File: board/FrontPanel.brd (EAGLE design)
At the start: 76.2 x 44.5 mm, 10 parts, among them J1 PINHD-1X2BIG

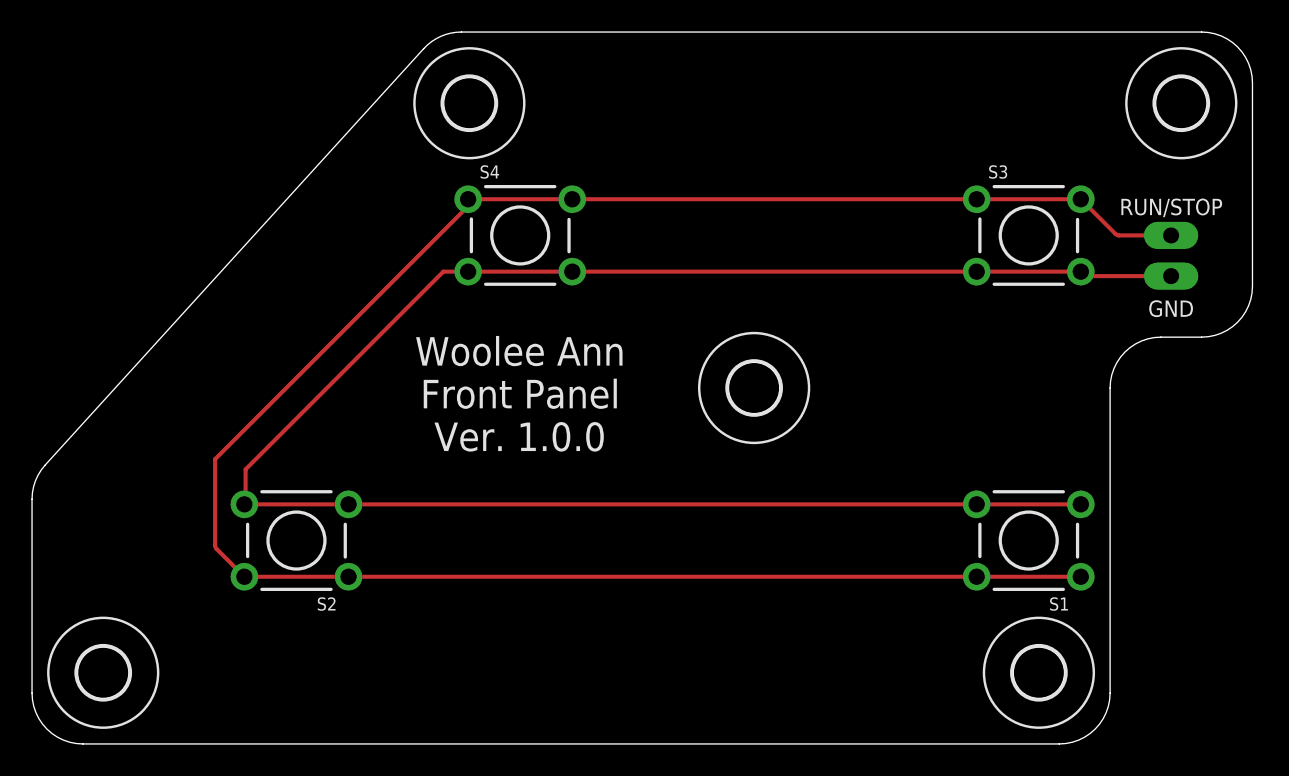
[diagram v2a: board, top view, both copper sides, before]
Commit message: Adjust front panel layout
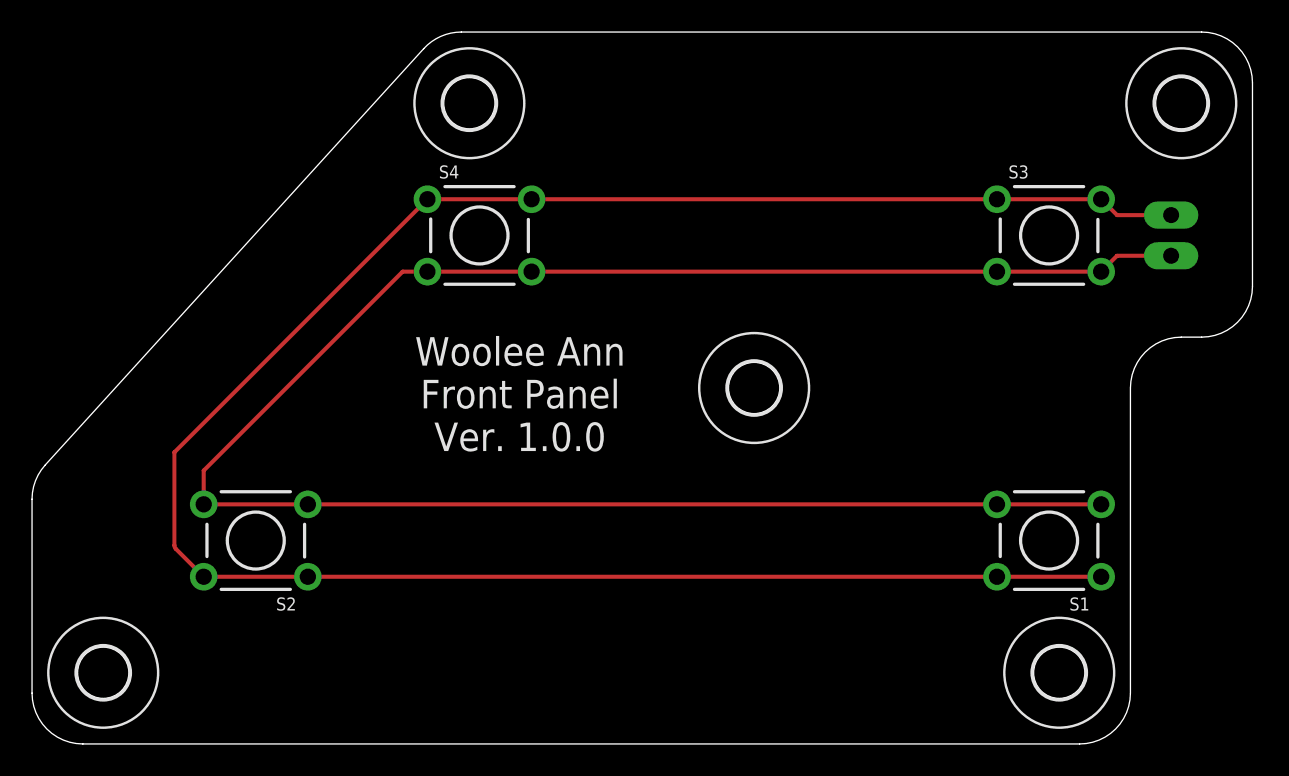
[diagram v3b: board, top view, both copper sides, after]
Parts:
- moved S2 2.54 mm to (14.0, 12.7)
- moved S4 2.54 mm to (27.9, 31.8)
- moved S1 1.27 mm to (63.5, 12.7)
- moved S3 1.27 mm to (63.5, 31.8)
- moved U$2 1.27 mm to (64.1, 4.45)
- moved J1 1.27 mm to (71.1, 31.8)
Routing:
- net N$2: track 117.4 -> 124.2 mm
- net N$1: track 127.9 -> 133.7 mm
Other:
- outline, holes or cut-outs redrawn
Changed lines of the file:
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@@
 <setting verticaltext="up"/>
 </settings>
-<grid distance="0.05" unitdist="inch" unit="inch" style="lines" multiple="1" display="yes" altdistance="0.025" altunitdist="inch" altunit="inch"/>
+<grid distance="0.05" unitdist="inch" unit="inch" style="lines" multiple="2" display="yes" altdistance="0.025" altunitdist="inch" altunit="inch"/>
 <layers>
 <layer number="1" name="Top" color="4" fill="1" visible="yes" active="yes"/>
@@
 <wire x1="0" y1="15.282521875" x2="0" y2="3.175" width="0" layer="20"/>
 <wire x1="0" y1="3.175" x2="3.175" y2="0" width="0" layer="20" curve="90"/>
-<wire x1="3.175" y1="0" x2="64.135" y2="0" width="0" layer="20"/>
-<wire x1="64.135" y1="0" x2="67.31" y2="3.175" width="0" layer="20" curve="90"/>
-<wire x1="67.31" y1="3.175" x2="67.31" y2="22.225" width="0" layer="20"/>
-<wire x1="67.31" y1="22.225" x2="70.485" y2="25.4" width="0" layer="20" curve="-90"/>
-<wire x1="70.485" y1="25.4" x2="73.025" y2="25.4" width="0" layer="20"/>
+<wire x1="3.175" y1="0" x2="65.405" y2="0" width="0" layer="20"/>
+<wire x1="65.405" y1="0" x2="68.58" y2="3.175" width="0" layer="20" curve="90"/>
+<wire x1="68.58" y1="3.175" x2="68.58" y2="22.225" width="0" layer="20"/>
+<wire x1="68.58" y1="22.225" x2="71.755" y2="25.4" width="0" layer="20" curve="-90"/>
+<wire x1="71.755" y1="25.4" x2="73.025" y2="25.4" width="0" layer="20"/>
 <wire x1="73.025" y1="25.4" x2="76.2" y2="28.575" width="0" layer="20" curve="90"/>
-<text x="71.12" y="33.02" size="1.016" layer="121" align="bottom-center">RUN/STOP</text>
-<text x="71.12" y="26.67" size="1.016" layer="121" align="bottom-center">GND</text>
+<text x="71.12" y="34.29" size="1.016" layer="122" rot="MR0" align="bottom-center">RUN/STOP</text>
+<text x="71.12" y="27.94" size="1.016" layer="122" rot="MR0" align="bottom-center">GND</text>
 <text x="30.48" y="25.4" size="1.778" layer="121" align="top-center">Woolee Ann
 Front Panel
@@
 </autorouter>
 <elements>
-<element name="S1" library="SaintGimp" package="TACTILE-SWITCH-6MM" value="SWITCH-MOMENTARY-6MM" x="62.23" y="12.7" rot="R180"/>
-<element name="S2" library="SaintGimp" package="TACTILE-SWITCH-6MM" value="SWITCH-MOMENTARY-6MM" x="16.51" y="12.7" rot="R180"/>
-<element name="S3" library="SaintGimp" package="TACTILE-SWITCH-6MM" value="SWITCH-MOMENTARY-6MM" x="62.23" y="31.75"/>
-<element name="S4" library="SaintGimp" package="TACTILE-SWITCH-6MM" value="SWITCH-MOMENTARY-6MM" x="30.48" y="31.75"/>
-<element name="J1" library="SaintGimp" package="1X02-BIG" value="PINHD-1X2BIG" x="71.12" y="30.48" smashed="yes" rot="R270"/>
+<element name="S1" library="SaintGimp" package="TACTILE-SWITCH-6MM" value="SWITCH-MOMENTARY-6MM" x="63.5" y="12.7" rot="R180"/>
+<element name="S2" library="SaintGimp" package="TACTILE-SWITCH-6MM" value="SWITCH-MOMENTARY-6MM" x="13.97" y="12.7" rot="R180"/>
+<element name="S3" library="SaintGimp" package="TACTILE-SWITCH-6MM" value="SWITCH-MOMENTARY-6MM" x="63.5" y="31.75"/>
+<element name="S4" library="SaintGimp" package="TACTILE-SWITCH-6MM" value="SWITCH-MOMENTARY-6MM" x="27.94" y="31.75"/>
+<element name="J1" library="SaintGimp" package="1X02-BIG" value="PINHD-1X2BIG" x="71.12" y="31.75" smashed="yes" rot="R270"/>
 <element name="U$1" library="holes" package="3,2" value="" x="4.445" y="4.445"/>
-<element name="U$2" library="holes" package="3,2" value="" x="62.865" y="4.445"/>
+<element name="U$2" library="holes" package="3,2" value="" x="64.135" y="4.445"/>
 <element name="U$3" library="holes" package="3,2" value="" x="27.305" y="40.005"/>
 <element name="U$4" library="holes" package="3,2" value="" x="71.755" y="40.005"/>
@@
 <contactref element="S4" pad="1"/>
 <contactref element="S4" pad="2"/>
-<wire x1="71.12" y1="31.75" x2="67.8733125" y2="31.75" width="0.254" layer="1"/>
-<wire x1="67.8733125" y1="31.75" x2="67.64880625" y2="31.84299375" width="0.254" layer="1" curve="-45"/>
-<wire x1="67.64880625" y1="31.84299375" x2="65.4812" y2="34.0106" width="0.254" layer="1"/>
-<wire x1="65.4812" y1="34.0106" x2="58.9788" y2="34.0106" width="0.254" layer="1"/>
-<wire x1="58.9788" y1="34.0106" x2="33.7312" y2="34.0106" width="0.254" layer="1"/>
-<wire x1="33.7312" y1="34.0106" x2="27.2288" y2="34.0106" width="0.254" layer="1"/>
-<wire x1="27.2288" y1="34.0106" x2="27.2288" y2="33.7103125" width="0.254" layer="1"/>
-<wire x1="27.2288" y1="33.7103125" x2="27.13580625" y2="33.48580625" width="0.254" layer="1" curve="-45"/>
-<wire x1="27.13580625" y1="33.48580625" x2="11.43" y2="17.78" width="0.254" layer="1"/>
-<wire x1="11.43" y1="17.78" x2="11.43" y2="12.3997125" width="0.254" layer="1"/>
-<wire x1="11.43" y1="12.3997125" x2="11.52299375" y2="12.17520625" width="0.254" layer="1" curve="45"/>
-<wire x1="11.52299375" y1="12.17520625" x2="13.2588" y2="10.4394" width="0.254" layer="1"/>
-<wire x1="13.2588" y1="10.4394" x2="19.7612" y2="10.4394" width="0.254" layer="1"/>
-<wire x1="58.9788" y1="10.4394" x2="19.7612" y2="10.4394" width="0.254" layer="1"/>
-<wire x1="58.9788" y1="10.4394" x2="65.4812" y2="10.4394" width="0.254" layer="1"/>
+<wire x1="66.7512" y1="34.0106" x2="60.2488" y2="34.0106" width="0.254" layer="1"/>
+<wire x1="60.2488" y1="34.0106" x2="31.1912" y2="34.0106" width="0.254" layer="1"/>
+<wire x1="31.1912" y1="34.0106" x2="24.6888" y2="34.0106" width="0.254" layer="1"/>
+<wire x1="8.89" y1="18.2118" x2="8.89" y2="12.3997125" width="0.254" layer="1"/>
+<wire x1="8.89" y1="12.3997125" x2="8.98299375" y2="12.17520625" width="0.254" layer="1" curve="45"/>
+<wire x1="8.98299375" y1="12.17520625" x2="10.7188" y2="10.4394" width="0.254" layer="1"/>
+<wire x1="10.7188" y1="10.4394" x2="17.2212" y2="10.4394" width="0.254" layer="1"/>
+<wire x1="60.2488" y1="10.4394" x2="17.2212" y2="10.4394" width="0.254" layer="1"/>
+<wire x1="60.2488" y1="10.4394" x2="66.7512" y2="10.4394" width="0.254" layer="1"/>
+<wire x1="71.12" y1="33.02" x2="67.7418" y2="33.02" width="0.254" layer="1"/>
+<wire x1="67.7418" y1="33.02" x2="66.7512" y2="34.0106" width="0.254" layer="1"/>
+<wire x1="24.6888" y1="34.0106" x2="8.89" y2="18.2118" width="0.254" layer="1"/>
 </signal>
 <signal name="N$2">
@@
 <contactref element="S1" pad="3"/>
 <contactref element="J1" pad="2"/>
-<wire x1="71.12" y1="29.21" x2="65.8921125" y2="29.21" width="0.254" layer="1"/>
-<wire x1="65.8921125" y1="29.21" x2="65.66760625" y2="29.30299375" width="0.254" layer="1" curve="-45"/>
-<wire x1="65.66760625" y1="29.30299375" x2="65.4812" y2="29.4894" width="0.254" layer="1"/>
-<wire x1="65.4812" y1="29.4894" x2="58.9788" y2="29.4894" width="0.254" layer="1"/>
-<wire x1="58.9788" y1="29.4894" x2="33.7312" y2="29.4894" width="0.254" layer="1"/>
-<wire x1="33.7312" y1="29.4894" x2="27.2288" y2="29.4894" width="0.254" layer="1"/>
-<wire x1="13.2588" y1="14.9606" x2="19.7612" y2="14.9606" width="0.254" layer="1"/>
-<wire x1="58.9788" y1="14.9606" x2="19.7612" y2="14.9606" width="0.254" layer="1"/>
-<wire x1="58.9788" y1="14.9606" x2="65.4812" y2="14.9606" width="0.254" layer="1"/>
-<wire x1="27.2288" y1="29.4894" x2="25.6794" y2="29.4894" width="0.254" layer="1"/>
-<wire x1="25.6794" y1="29.4894" x2="13.335" y2="17.145" width="0.254" layer="1"/>
-<wire x1="13.335" y1="17.145" x2="13.335" y2="15.0368" width="0.254" layer="1"/>
-<wire x1="13.335" y1="15.0368" x2="13.2588" y2="14.9606" width="0.254" layer="1"/>
+<wire x1="66.7512" y1="29.4894" x2="60.2488" y2="29.4894" width="0.254" layer="1"/>
+<wire x1="60.2488" y1="29.4894" x2="31.1912" y2="29.4894" width="0.254" layer="1"/>
+<wire x1="31.1912" y1="29.4894" x2="24.6888" y2="29.4894" width="0.254" layer="1"/>
+<wire x1="10.7188" y1="14.9606" x2="17.2212" y2="14.9606" width="0.254" layer="1"/>
+<wire x1="60.2488" y1="14.9606" x2="17.2212" y2="14.9606" width="0.254" layer="1"/>
+<wire x1="60.2488" y1="14.9606" x2="66.7512" y2="14.9606" width="0.254" layer="1"/>
+<wire x1="10.795" y1="15.0368" x2="10.7188" y2="14.9606" width="0.254" layer="1"/>
+<wire x1="71.12" y1="30.48" x2="67.7418" y2="30.48" width="0.254" layer="1"/>
+<wire x1="67.7418" y1="30.48" x2="66.7512" y2="29.4894" width="0.254" layer="1"/>
+<wire x1="24.6888" y1="29.4894" x2="23.1394" y2="29.4894" width="0.254" layer="1"/>
+<wire x1="23.1394" y1="29.4894" x2="10.7188" y2="17.0688" width="0.254" layer="1"/>
+<wire x1="10.7188" y1="17.0688" x2="10.7188" y2="14.9606" width="0.254" layer="1"/>
 </signal>
 </signals>

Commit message: Spread out front panel buttons, flip terminal silkscreen to back
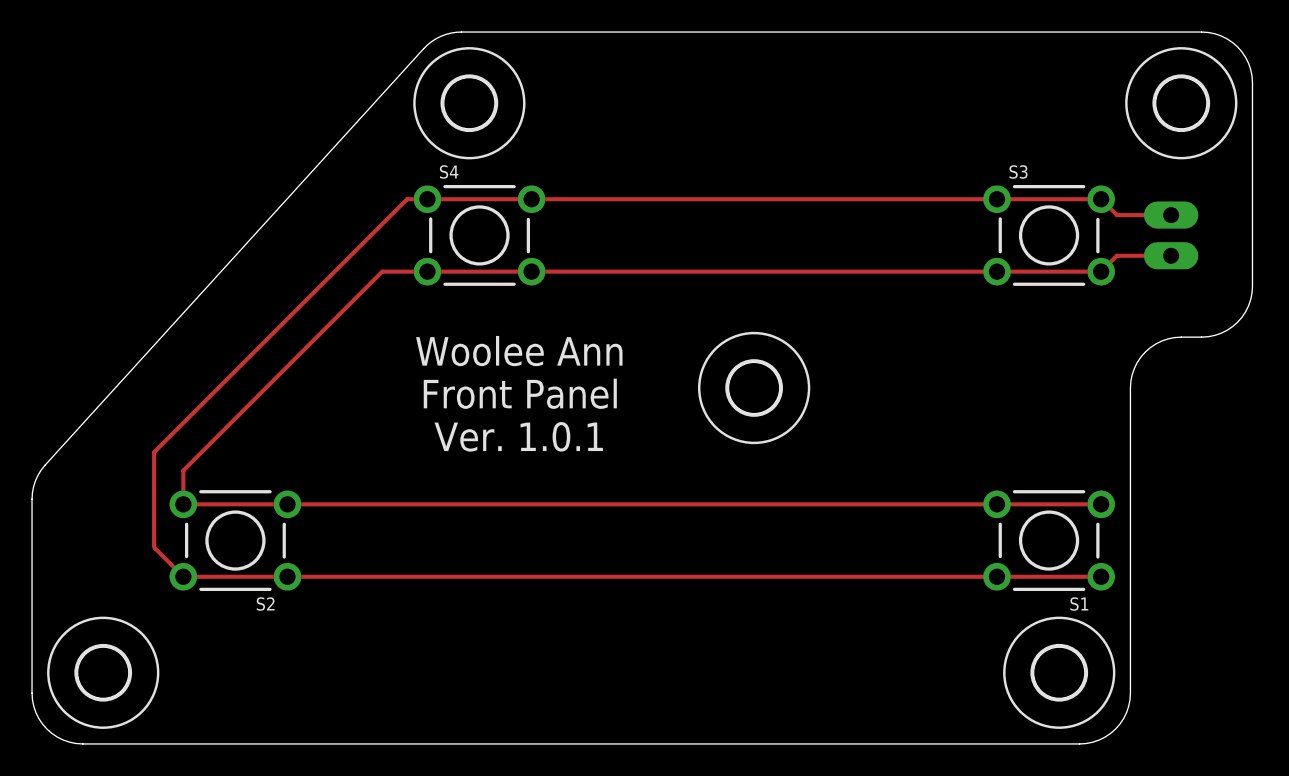
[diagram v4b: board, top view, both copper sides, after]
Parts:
- moved S2 1.27 mm to (12.7, 12.7)
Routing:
- net N$1: track 133.7 -> 136.3 mm
- net N$2: track 124.2 -> 126.7 mm
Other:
- board text added: "Woolee Ann Front Panel Ver. 1.0.1"
- board text removed: "Woolee Ann Front Panel Ver. 1.0.0"
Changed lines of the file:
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@@
 <text x="30.48" y="25.4" size="1.778" layer="121" align="top-center">Woolee Ann
 Front Panel
-Ver. 1.0.0</text>
+Ver. 1.0.1</text>
 </plain>
 <attributes>
@@
 <elements>
 <element name="S1" library="SaintGimp" package="TACTILE-SWITCH-6MM" value="SWITCH-MOMENTARY-6MM" x="63.5" y="12.7" rot="R180"/>
-<element name="S2" library="SaintGimp" package="TACTILE-SWITCH-6MM" value="SWITCH-MOMENTARY-6MM" x="13.97" y="12.7" rot="R180"/>
+<element name="S2" library="SaintGimp" package="TACTILE-SWITCH-6MM" value="SWITCH-MOMENTARY-6MM" x="12.7" y="12.7" rot="R180"/>
 <element name="S3" library="SaintGimp" package="TACTILE-SWITCH-6MM" value="SWITCH-MOMENTARY-6MM" x="63.5" y="31.75"/>
 <element name="S4" library="SaintGimp" package="TACTILE-SWITCH-6MM" value="SWITCH-MOMENTARY-6MM" x="27.94" y="31.75"/>
@@
 <wire x1="60.2488" y1="34.0106" x2="31.1912" y2="34.0106" width="0.254" layer="1"/>
 <wire x1="31.1912" y1="34.0106" x2="24.6888" y2="34.0106" width="0.254" layer="1"/>
-<wire x1="8.89" y1="18.2118" x2="8.89" y2="12.3997125" width="0.254" layer="1"/>
-<wire x1="8.89" y1="12.3997125" x2="8.98299375" y2="12.17520625" width="0.254" layer="1" curve="45"/>
-<wire x1="8.98299375" y1="12.17520625" x2="10.7188" y2="10.4394" width="0.254" layer="1"/>
-<wire x1="10.7188" y1="10.4394" x2="17.2212" y2="10.4394" width="0.254" layer="1"/>
-<wire x1="60.2488" y1="10.4394" x2="17.2212" y2="10.4394" width="0.254" layer="1"/>
+<wire x1="7.62" y1="18.2118" x2="7.62" y2="12.3997125" width="0.254" layer="1"/>
+<wire x1="7.62" y1="12.3997125" x2="7.71299375" y2="12.17520625" width="0.254" layer="1" curve="45"/>
+<wire x1="7.71299375" y1="12.17520625" x2="9.4488" y2="10.4394" width="0.254" layer="1"/>
+<wire x1="9.4488" y1="10.4394" x2="15.9512" y2="10.4394" width="0.254" layer="1"/>
+<wire x1="60.2488" y1="10.4394" x2="15.9512" y2="10.4394" width="0.254" layer="1"/>
 <wire x1="60.2488" y1="10.4394" x2="66.7512" y2="10.4394" width="0.254" layer="1"/>
 <wire x1="71.12" y1="33.02" x2="67.7418" y2="33.02" width="0.254" layer="1"/>
 <wire x1="67.7418" y1="33.02" x2="66.7512" y2="34.0106" width="0.254" layer="1"/>
-<wire x1="24.6888" y1="34.0106" x2="8.89" y2="18.2118" width="0.254" layer="1"/>
+<wire x1="24.6888" y1="34.0106" x2="23.4188" y2="34.0106" width="0.254" layer="1"/>
+<wire x1="23.4188" y1="34.0106" x2="7.62" y2="18.2118" width="0.254" layer="1"/>
 </signal>
 <signal name="N$2">
@@
 <wire x1="60.2488" y1="29.4894" x2="31.1912" y2="29.4894" width="0.254" layer="1"/>
 <wire x1="31.1912" y1="29.4894" x2="24.6888" y2="29.4894" width="0.254" layer="1"/>
-<wire x1="10.7188" y1="14.9606" x2="17.2212" y2="14.9606" width="0.254" layer="1"/>
-<wire x1="60.2488" y1="14.9606" x2="17.2212" y2="14.9606" width="0.254" layer="1"/>
+<wire x1="9.4488" y1="14.9606" x2="15.9512" y2="14.9606" width="0.254" layer="1"/>
+<wire x1="60.2488" y1="14.9606" x2="15.9512" y2="14.9606" width="0.254" layer="1"/>
 <wire x1="60.2488" y1="14.9606" x2="66.7512" y2="14.9606" width="0.254" layer="1"/>
-<wire x1="10.795" y1="15.0368" x2="10.7188" y2="14.9606" width="0.254" layer="1"/>
+<wire x1="9.525" y1="15.0368" x2="9.4488" y2="14.9606" width="0.254" layer="1"/>
 <wire x1="71.12" y1="30.48" x2="67.7418" y2="30.48" width="0.254" layer="1"/>
 <wire x1="67.7418" y1="30.48" x2="66.7512" y2="29.4894" width="0.254" layer="1"/>
-<wire x1="24.6888" y1="29.4894" x2="23.1394" y2="29.4894" width="0.254" layer="1"/>
-<wire x1="23.1394" y1="29.4894" x2="10.7188" y2="17.0688" width="0.254" layer="1"/>
-<wire x1="10.7188" y1="17.0688" x2="10.7188" y2="14.9606" width="0.254" layer="1"/>
+<wire x1="24.6888" y1="29.4894" x2="21.8694" y2="29.4894" width="0.254" layer="1"/>
+<wire x1="9.4488" y1="17.0688" x2="9.4488" y2="14.9606" width="0.254" layer="1"/>
+<wire x1="21.8694" y1="29.4894" x2="9.4488" y2="17.0688" width="0.254" layer="1"/>
 </signal>
 </signals>
